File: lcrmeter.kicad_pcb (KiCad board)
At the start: 2 copper layers, 63.4 x 75.5 mm, 35 parts, among them J1 inductor, J2 inductor, J3 gen, J4 1,5V, J5 gen, J6 OSC, J7 OSC, SW1 power, SW2 +, SW3 -, SW4 ok, SW5 back, U1 MCP47, U2 STM32F103C8Tx, Y1 8Mhz

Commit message: assigned footprints, fixed schematic, a little done PCB
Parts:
- removed DIS1: nokia5110_LCD, Moje:LCD_5110
- removed L1: 10u, Inductors_SMD:L_0805_HandSoldering
- added C10: 100n, Capacitor_SMD:C_0603_1608Metric_Pad1.05x0.95mm_HandSolder, B.Cu at (137.4, 118.5)
- added C11: 2u2, Capacitor_SMD:C_0805_2012Metric_Pad1.15x1.40mm_HandSolder, B.Cu at (126.5, 177.5)
- added C12: 100n, Capacitor_SMD:C_0603_1608Metric_Pad1.05x0.95mm_HandSolder, B.Cu at (91.6, 141.0)
- added C13: 100n, Capacitor_SMD:C_0603_1608Metric_Pad1.05x0.95mm_HandSolder, B.Cu at (162.6, 142.6)
- added C14: 100n, Capacitor_SMD:C_0603_1608Metric_Pad1.05x0.95mm_HandSolder, B.Cu at (103.2, 155.9)
- added C15: 100n, Capacitor_SMD:C_0603_1608Metric_Pad1.05x0.95mm_HandSolder, B.Cu at (145.4, 166.1)
- added C8: 10u, Capacitor_SMD:C_0603_1608Metric_Pad1.05x0.95mm_HandSolder, B.Cu at (168.5, 138.2)
- added C9: 100n, Capacitor_SMD:C_0603_1608Metric_Pad1.05x0.95mm_HandSolder, B.Cu at (91.2, 148.7)
- added D1: BAT54S, Package_TO_SOT_SMD:SOT-23, B.Cu at (119.4, 105.9)
- added D2: BAT54S, Package_TO_SOT_SMD:SOT-23, B.Cu at (156.0, 109.7)
- added D3: BAT54S, Package_TO_SOT_SMD:SOT-23, B.Cu at (158.0, 114.0)
- added D4: BAT54S, Package_TO_SOT_SMD:SOT-23, B.Cu at (141.8, 106.4)
- added D5: BAT54S, Package_TO_SOT_SMD:SOT-23, B.Cu at (157.5, 106.2)
- added R10: 10k, Resistor_SMD:R_0603_1608Metric_Pad1.05x0.95mm_HandSolder, B.Cu at (133.0, 161.6)
- added R11: 10k, Resistor_SMD:R_0603_1608Metric_Pad1.05x0.95mm_HandSolder, B.Cu at (167.0, 141.0)
- added R12: 10k, Resistor_SMD:R_0603_1608Metric_Pad1.05x0.95mm_HandSolder, B.Cu at (87.9, 149.7)
- added R13: 10k, Resistor_SMD:R_0603_1608Metric_Pad1.05x0.95mm_HandSolder, B.Cu at (145.5, 141.1)
- added R14: 22, Resistor_SMD:R_0805_2012Metric_Pad1.15x1.40mm_HandSolder, B.Cu at (161.3, 119.6)
- added R15: 1k5, Resistor_SMD:R_0805_2012Metric_Pad1.15x1.40mm_HandSolder, B.Cu at (92.2, 163.6)
- added R16: 22, Resistor_SMD:R_0805_2012Metric_Pad1.15x1.40mm_HandSolder, B.Cu at (84.6, 153.1)
- added R17: 100, Resistor_SMD:R_0805_2012Metric_Pad1.15x1.40mm_HandSolder, B.Cu at (162.3, 114.3)
- added R18: 100, Resistor_SMD:R_0805_2012Metric_Pad1.15x1.40mm_HandSolder, B.Cu at (155.9, 163.3)
- added R9: 10k, Resistor_SMD:R_0603_1608Metric_Pad1.05x0.95mm_HandSolder, B.Cu at (151.3, 154.4)
- added U3: OLED, footprints:OLED_128x64, F.Cu at (153.4, 106.4)
- added U4: 74HC14, Package_SO:SOIC-14_3.9x8.7mm_P1.27mm, B.Cu at (126.3, 123.7)
- BT1, BT2: footprint Battery_Holders:Keystone_2466_1xAAA -> Battery:BatteryHolder_Keystone_2466_1xAAA
- C1, C2: footprint Capacitors_SMD:C_0805_HandSoldering -> Capacitor_SMD:C_0805_2012Metric_Pad1.15x1.40mm_HandSolder
- C3, C4, C5, C6: footprint Capacitors_SMD:C_0805_HandSoldering -> Capacitor_SMD:C_0603_1608Metric_Pad1.05x0.95mm_HandSolder; moved to B.Cu
- C7: value 10n -> 100n; footprint Capacitors_SMD:C_0805_HandSoldering -> Capacitor_SMD:C_0603_1608Metric_Pad1.05x0.95mm_HandSolder; moved to B.Cu
- J1: value inductor -> LCR_input; footprint Pin_Headers:Pin_Header_Straight_1x04_Pitch2.54mm -> Connector_PinHeader_2.54mm:PinHeader_1x04_P2.54mm_Vertical
- J2: value inductor -> LCR_input; footprint Socket_Strips:Socket_Strip_Straight_1x04_Pitch2.54mm -> Connector_PinSocket_2.54mm:PinSocket_1x04_P2.54mm_Vertical
- J3: value gen -> Conn_01x06; footprint Socket_Strips:Socket_Strip_Straight_1x02_Pitch2.54mm -> Connector_PinHeader_2.54mm:PinHeader_1x06_P2.54mm_Vertical
- J4: value 1,5V -> USB_B_Micro; footprint Socket_Strips:Socket_Strip_Straight_1x02_Pitch2.54mm -> Connector_USB:USB_Micro-B_Molex_47346-0001
- J5: value gen -> OSCILLOSCOPE; footprint Pin_Headers:Pin_Header_Straight_1x02_Pitch2.54mm -> footprints:BNC TE CONNECTIVITY 5-1634503
- J6: value OSC -> misc; footprint Socket_Strips:Socket_Strip_Straight_1x02_Pitch2.54mm -> Connector_PinSocket_2.54mm:PinSocket_1x06_P2.54mm_Vertical
- J7: value OSC -> misc; footprint Pin_Headers:Pin_Header_Straight_1x02_Pitch2.54mm -> Connector_PinHeader_2.54mm:PinHeader_1x06_P2.54mm_Vertical
- L2: footprint Inductors_SMD:L_0805_HandSoldering -> Inductor_SMD:L_0805_2012Metric_Pad1.15x1.40mm_HandSolder; moved to B.Cu
- R1: value R -> 100; footprint Resistors_SMD:R_0805_HandSoldering -> Resistor_SMD:R_0805_2012Metric_Pad1.15x1.40mm_HandSolder; moved to B.Cu
- R2: value 4K7 -> 10k; footprint Resistors_SMD:R_0805_HandSoldering -> Resistor_SMD:R_0603_1608Metric_Pad1.05x0.95mm_HandSolder; moved to B.Cu
- R3, R4, R5, R6: footprint Resistors_SMD:R_0805_HandSoldering -> Resistor_SMD:R_0603_1608Metric_Pad1.05x0.95mm_HandSolder
- R7, R8: footprint Resistors_SMD:R_0805_HandSoldering -> Resistor_SMD:R_0805_2012Metric_Pad1.15x1.40mm_HandSolder; moved to B.Cu
- SW1: footprint Pin_Headers:Pin_Header_Straight_1x03_Pitch2.54mm -> Connector_PinHeader_2.54mm:PinHeader_1x03_P2.54mm_Vertical
- SW2, SW3, SW4, SW5: footprint Buttons_Switches_SMD:SW_SPST_REED_CT05-XXXX-G1 -> Button_Switch_SMD:SW_SPST_REED_CT05-XXXX-G1
- U1: footprint Housings_SSOP:TSSOP-8_4.4x3mm_Pitch0.65mm -> Package_SO:TSSOP-8_4.4x3mm_P0.65mm; moved to B.Cu
- U2: footprint Housings_QFP:LQFP-48_7x7mm_Pitch0.5mm -> Package_QFP:LQFP-48_7x7mm_P0.5mm; moved to B.Cu
- Y1: footprint Crystals:Crystal_HC49-U_Vertical -> Crystal:Crystal_HC49-U_Vertical; moved to F.Cu
- moved C6 73.5 mm to (99.8, 154.4), turned to 0 degrees
- moved R4 70.5 mm to (129.3, 156.0), turned to 0 degrees
- moved C5 69.5 mm to (106.3, 162.0)
- moved L2 66.6 mm to (112.8, 177.5), turned to 0 degrees
- moved C7 65.0 mm to (106.3, 163.5), turned to 0 degrees
- moved SW2 61.3 mm to (140.7, 137.2), turned to 0 degrees
- moved R3 60.3 mm to (138.1, 153.9), turned to 0 degrees
- moved SW3 60.2 mm to (140.7, 144.8), turned to 0 degrees
- moved BT1 59.7 mm to (126.1, 144.3), turned to 90 degrees
- moved C4 58.8 mm to (109.7, 165.5), turned to 0 degrees
- moved J5 56.5 mm to (169.9, 102.4), turned to 0 degrees
- moved R2 40.5 mm to (149.6, 109.6), turned to 270 degrees
- moved U1 39.4 mm to (138.4, 111.5)
- moved SW4 38.0 mm to (154.9, 141.2), turned to 0 degrees
- moved R6 37.3 mm to (149.5, 135.1)
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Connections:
- J1 pad 1: Net-(J1-Pad1) -> /ADC_2
- J1 pad 2: Net-(J1-Pad1) -> /ADC_2
- J2 pad 1: Net-(J1-Pad1) -> /ADC_2
- J2 pad 2: Net-(J1-Pad1) -> /ADC_2
- J3 pad 1: GND -> VCC
- J4 pad 1: +1V5 -> /VBUS
- J4 pad 2: +1V5 -> Net-(J4-Pad2)
- J5 pad 1: Net-(J3-Pad2) -> Net-(J5-Pad1)
- J6 pad 1: OSC -> /PWM_OUT
- J6 pad 2: GND -> /8_MHz_OUT
- J7 pad 1: OSC -> /PWM_OUT
- J7 pad 2: GND -> /8_MHz_OUT
- R1 pad 1: Net-(J3-Pad2) -> /ADC_1
- R1 pad 2: Net-(J1-Pad1) -> /ADC_2
- R2 pad 1: VCC -> GND
- R3 pad 1: Net-(R3-Pad1) -> GND
- R3 pad 2: GND -> Net-(R3-Pad2)
- R4 pad 1: Net-(R4-Pad1) -> VCC
- R4 pad 2: GND -> Net-(R10-Pad2)
- R5 pad 1: Net-(R5-Pad1) -> VCC
- R5 pad 2: GND -> Net-(R11-Pad2)
- R6 pad 1: Net-(R6-Pad1) -> VCC
- R6 pad 2: GND -> Net-(R12-Pad2)
- R7 pad 2: Net-(R7-Pad2) -> /I2C_SCL
- R8 pad 2: Net-(R8-Pad2) -> /I2C_SDA
- SW1 pad 3: Net-(L1-Pad2) -> VCC
- SW2 pad 1: Net-(R3-Pad1) -> GND
- SW2 pad 2: VCC -> Net-(R12-Pad2)
- SW3 pad 1: Net-(R4-Pad1) -> GND
- SW3 pad 2: VCC -> Net-(R13-Pad2)
- SW4 pad 1: Net-(R5-Pad1) -> GND
- SW4 pad 2: VCC -> Net-(R10-Pad2)
- SW5 pad 1: Net-(R6-Pad1) -> GND
- SW5 pad 2: VCC -> Net-(R11-Pad2)
- U1 pad 3: Net-(J3-Pad2) -> /ADC_1
- U1 pad 6: GND -> /LATCH
- U1 pad 7: Net-(R8-Pad2) -> /I2C_SCL
- U1 pad 8: Net-(R7-Pad2) -> /I2C_SDA
- U2 pad 1: (no net) -> VCC
- U2 pad 12: Net-(DIS1-Pad1) -> /BUTTON_OK
- U2 pad 13: Net-(DIS1-Pad3) -> /BUTTON_BACK
- U2 pad 14: Net-(DIS1-Pad2) -> /BUTTON_-
- U2 pad 15: Net-(DIS1-Pad5) -> /BUTTON_+
- U2 pad 16: Net-(DIS1-Pad4) -> (no net)
- U2 pad 17: OSC -> /OSCILLOSCOPE
- U2 pad 18: Net-(J1-Pad1) -> /ADC_1
- U2 pad 19: Net-(J3-Pad2) -> /ADC_2
- U2 pad 20: GND -> Net-(R2-Pad2)
- U2 pad 21: (no net) -> Net-(U2-Pad21)
- U2 pad 22: (no net) -> Net-(U2-Pad22)
- U2 pad 29: (no net) -> /8_MHz_OUT
- U2 pad 30: (no net) -> /PWM_OUT
- U2 pad 31: (no net) -> /VBUS
- U2 pad 32: (no net) -> /USB_-
- U2 pad 33: Net-(R3-Pad1) -> /USB_+
- U2 pad 34: Net-(R4-Pad1) -> Net-(J3-Pad2)
- U2 pad 37: Net-(R5-Pad1) -> Net-(J3-Pad3)
- U2 pad 38: Net-(R6-Pad1) -> /USB_EN
- U2 pad 39: (no net) -> /SWO
- U2 pad 41: (no net) -> /LATCH
- U2 pad 42: Net-(R8-Pad2) -> /I2C_SCL
- U2 pad 43: Net-(R7-Pad2) -> /I2C_SDA
- U2 pad 44: GND -> Net-(R3-Pad2)
- U2 pad 7: Net-(R2-Pad2) -> /RST
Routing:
- net GND: track 376.2 -> 0.00 mm, vias 2 -> 0
- net VCC: track 142.6 -> 0.00 mm
- net +1V5: track 77.9 -> 0.00 mm
- net Net-(J3-Pad2): track 56.3 -> 0.00 mm, vias 3 -> 0
- net Net-(R3-Pad1): track 51.8 -> 0.00 mm, vias 3 -> 0
- net Net-(J1-Pad1): track 50.9 -> 0.00 mm, vias 2 -> 0
- net Net-(R4-Pad1): track 50.4 -> 0.00 mm, vias 2 -> 0
- net Net-(R5-Pad1): track 42.4 -> 0.00 mm, vias 2 -> 0
- net Net-(R6-Pad1): track 41.3 -> 0.00 mm, vias 2 -> 0
- net OSC: track 37.3 -> 0.00 mm, vias 1 -> 0
- net VDDA: track 32.6 -> 0.00 mm, vias 4 -> 0
- net Net-(DIS1-Pad1): track 31.4 -> 0.00 mm
- net Net-(DIS1-Pad4): track 27.5 -> 0.00 mm
- net Net-(R7-Pad2): track 25.6 -> 0.00 mm
- net Net-(DIS1-Pad5): track 22.8 -> 0.00 mm
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- removed copper zone on B.Cu, net GND
- removed copper zone on F.Cu, net GND
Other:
- board outline removed
- net class Default: via_dia 0.6 -> 0.8
- rule pad_to_mask_clearance: 0.1 -> 0
- board text removed: "+"
- board text removed: "-"
- board text removed: "1,5 V"
- board text removed: "BACK"
- board text removed: "GENERATOR"
- board text removed: "INDUCTOR"
- board text removed: "OK"
- board text removed: "OSCILISCOPE"

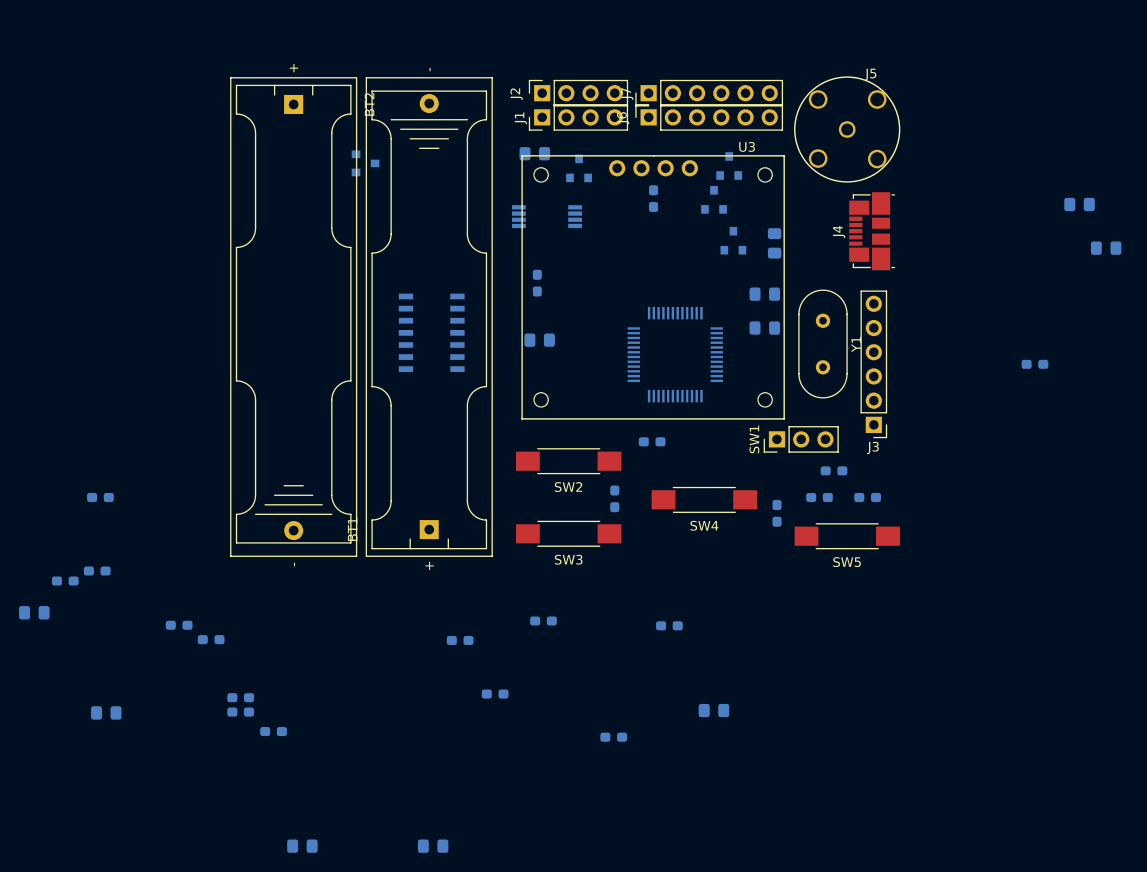
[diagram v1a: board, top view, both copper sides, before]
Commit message: started routing added voltage divider for measuring supply foltage
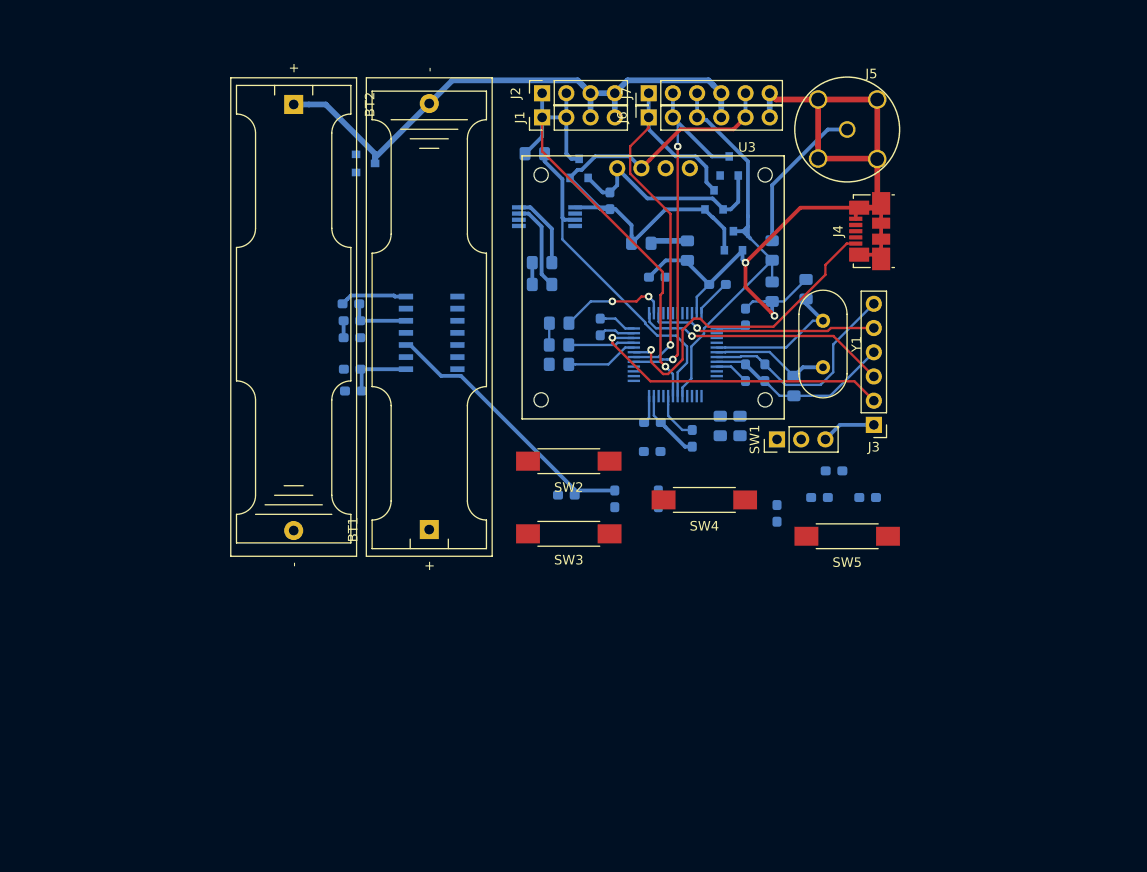
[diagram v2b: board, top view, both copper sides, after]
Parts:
- added R19: 20k, Resistor_SMD:R_0805_2012Metric_Pad1.15x1.40mm_HandSolder, B.Cu at (158.7, 133.5)
- added R20: 10k, Resistor_SMD:R_0805_2012Metric_Pad1.15x1.40mm_HandSolder, B.Cu at (156.6, 133.5)
- moved C9 73.0 mm to (159.3, 122.0), turned to 90 degrees
- moved L2 72.6 mm to (148.3, 114.3)
- moved C11 67.9 mm to (153.2, 115.1), turned to 270 degrees
- moved C5 66.2 mm to (156.3, 118.6), turned to 180 degrees
- moved C7 63.8 mm to (159.3, 127.9), turned to 90 degrees
- moved C6 63.4 mm to (145.0, 109.8), turned to 90 degrees
- moved R15 62.7 mm to (139.7, 122.7), turned to 180 degrees
- moved R16 61.8 mm to (139.7, 125.0)
- moved C4 54.6 mm to (144.0, 123.1), turned to 270 degrees
- moved R18 44.4 mm to (162.1, 119.4), turned to 270 degrees
- moved R10 41.9 mm to (118.0, 122.4), turned to 180 degrees
- moved C3 40.6 mm to (149.5, 133.1), turned to 0 degrees
- moved R3 38.0 mm to (150.0, 117.9)
- moved R12 37.4 mm to (118.0, 127.5), turned to 180 degrees
- moved C1 35.5 mm to (164.3, 129.3), turned to 270 degrees
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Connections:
- J4 pad 4: (no net) -> Net-(J4-Pad4)
- SW1 pad 1: (no net) -> Net-(SW1-Pad1)
- U1 pad 4: (no net) -> Net-(U1-Pad4)
- U2 pad 10: (no net) -> Net-(U2-Pad10)
- U2 pad 11: (no net) -> Net-(R19-Pad2)
- U2 pad 16: (no net) -> Net-(U2-Pad16)
- U2 pad 2: (no net) -> Net-(U2-Pad2)
- U2 pad 25: (no net) -> Net-(U2-Pad25)
- U2 pad 26: (no net) -> Net-(U2-Pad26)
- U2 pad 27: (no net) -> Net-(U2-Pad27)
- U2 pad 28: (no net) -> Net-(U2-Pad28)
- U2 pad 3: (no net) -> Net-(U2-Pad3)
- U2 pad 4: (no net) -> Net-(U2-Pad4)
- U2 pad 40: (no net) -> Net-(U2-Pad40)
- U2 pad 45: (no net) -> Net-(U2-Pad45)
- U2 pad 46: (no net) -> Net-(U2-Pad46)
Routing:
- net GND: track 0.00 -> 160.7 mm, vias 0 -> 2
- net VCC: track 0.00 -> 75.3 mm
- net +1V5: track 0.00 -> 61.3 mm
- net /ADC_2: track 0.00 -> 52.7 mm, vias 0 -> 1
- net /PWM_OUT: track 0.00 -> 45.0 mm, vias 0 -> 1
- net /OSCILLOSCOPE: track 0.00 -> 44.4 mm
- net /8_MHz_OUT: track 0.00 -> 40.2 mm, vias 0 -> 2
- net /ADC_1: track 0.00 -> 34.6 mm
- net /VBUS: track 0.00 -> 34.0 mm, vias 0 -> 1
- net Net-(J3-Pad2): track 0.00 -> 32.8 mm, vias 0 -> 1
- net Net-(C15-Pad1): track 0.00 -> 29.0 mm
- net Net-(J3-Pad3): track 0.00 -> 26.8 mm, vias 0 -> 1
- net /SWO: track 0.00 -> 24.1 mm, vias 0 -> 1
- net /RST: track 0.00 -> 23.0 mm
- net Net-(J5-Pad1): track 0.00 -> 16.1 mm
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
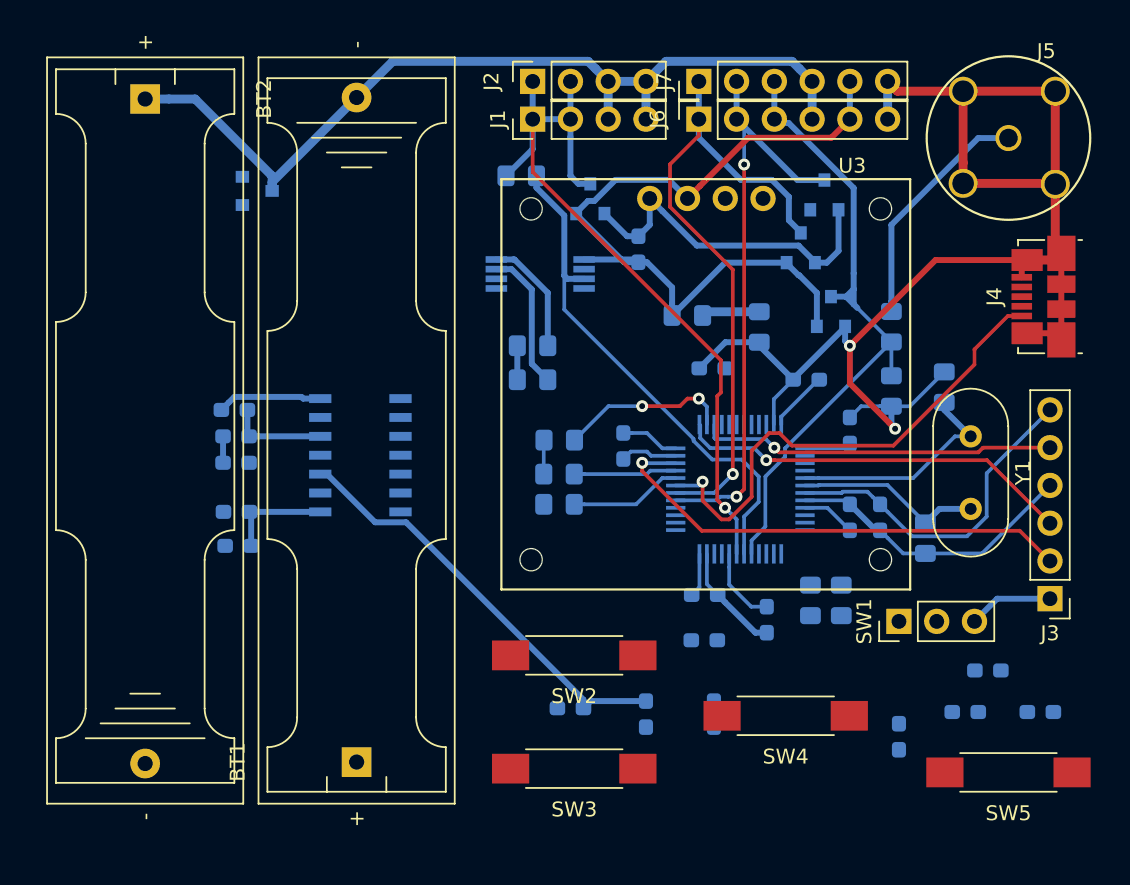
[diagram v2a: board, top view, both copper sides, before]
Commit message: fixed resistors value, PCB done!
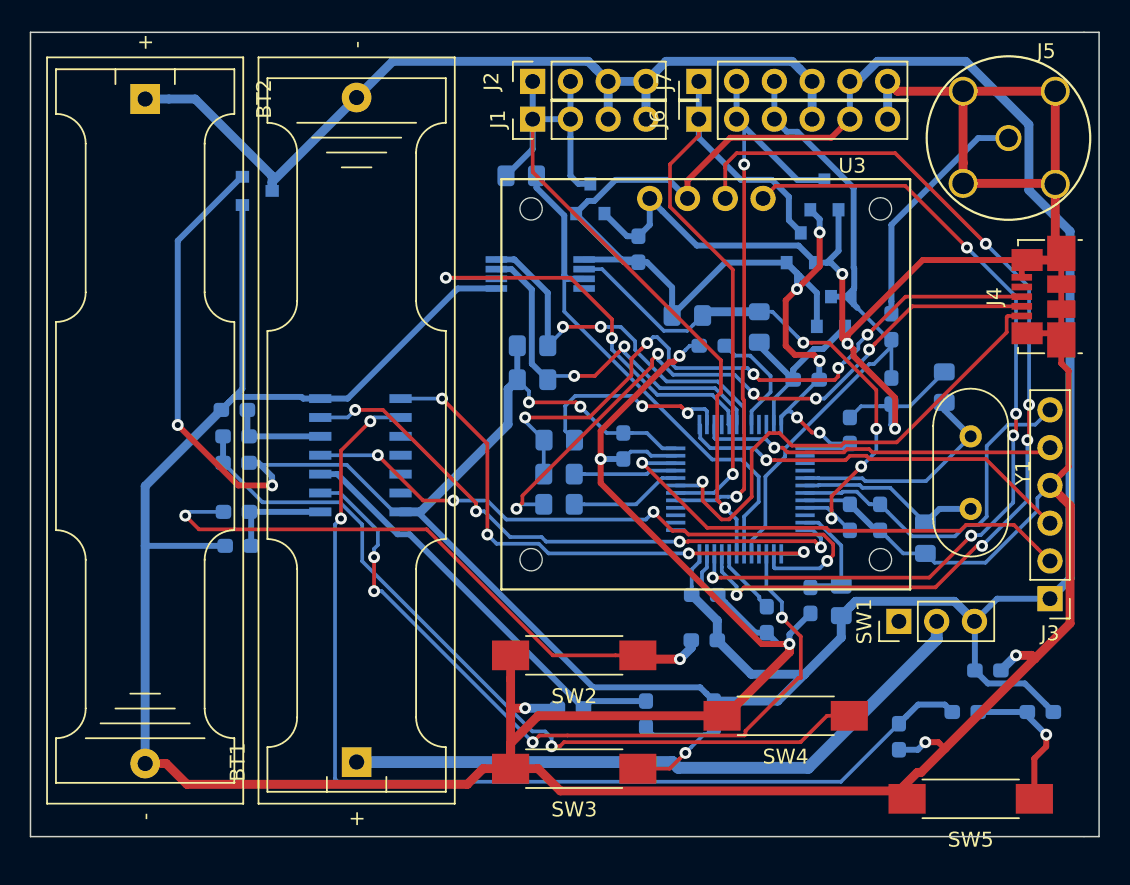
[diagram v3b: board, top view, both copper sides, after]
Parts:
- R17, R18: value 100 -> 10k; footprint Resistor_SMD:R_0805_2012Metric_Pad1.15x1.40mm_HandSolder -> Resistor_SMD:R_0603_1608Metric_Pad1.05x0.95mm_HandSolder
- R20: footprint Resistor_SMD:R_0805_2012Metric_Pad1.15x1.40mm_HandSolder -> Resistor_SMD:R_0603_1608Metric_Pad1.05x0.95mm_HandSolder
- moved SW5 3.10 mm to (167.4, 146.8)
- moved R3 1.52 mm to (150.0, 116.3)
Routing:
- net GND: track 160.7 -> 390.1 mm, vias 2 -> 9
- net VCC: track 75.3 -> 276.2 mm, vias 0 -> 9
- net Net-(C13-Pad1): track 0.00 -> 71.1 mm, vias 0 -> 2
- net Net-(U2-Pad21): track 0.00 -> 66.5 mm, vias 0 -> 5
- net Net-(U2-Pad22): track 0.00 -> 58.3 mm, vias 0 -> 5
- net /BUTTON_+: track 0.00 -> 53.2 mm, vias 0 -> 4
- net Net-(R10-Pad2): track 1.78 -> 54.4 mm, vias 0 -> 1
- net Net-(J4-Pad2): track 0.00 -> 45.0 mm, vias 0 -> 5
- net Net-(BT1-Pad1): track 0.00 -> 44.0 mm
- net /BUTTON_-: track 0.00 -> 43.4 mm, vias 0 -> 4
- net Net-(J4-Pad3): track 2.29 -> 45.2 mm, vias 0 -> 5
- net Net-(R12-Pad2): track 0.00 -> 41.5 mm, vias 0 -> 2
- net /BUTTON_OK: track 0.00 -> 40.0 mm, vias 0 -> 4
- net /BUTTON_BACK: track 0.00 -> 36.6 mm, vias 0 -> 4
- net VDDA: track 7.56 -> 37.9 mm, vias 0 -> 4
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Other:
- board outline added: 71.9 x 54.1 mm

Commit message: deleted 1,5V diode protection, added op-amp for 1,5V(optional), added zones
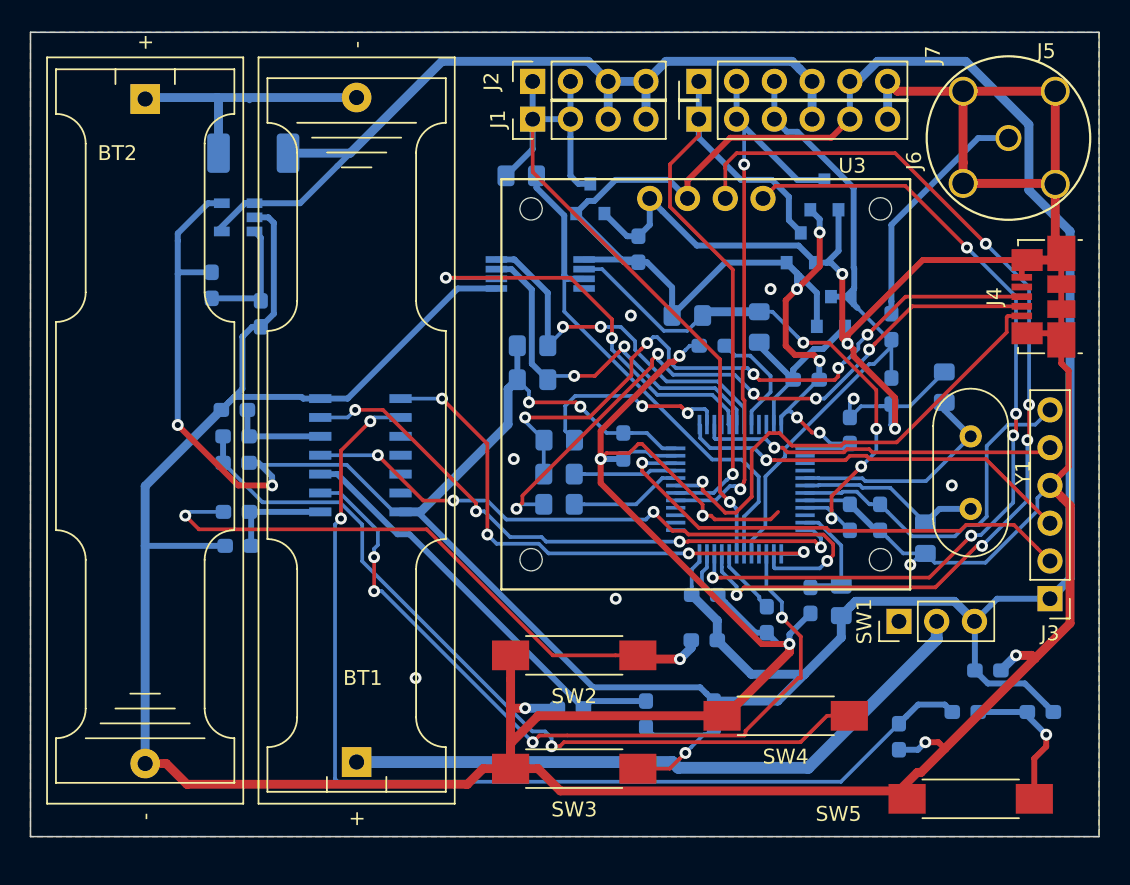
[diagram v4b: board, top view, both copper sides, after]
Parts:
- removed D1: BAT54S, Package_TO_SOT_SMD:SOT-23
- added R21: 0, Resistor_SMD:R_2010_5025Metric_Pad1.52x2.65mm_HandSolder, B.Cu at (119.1, 103.4)
- added R22: 10k, Resistor_SMD:R_0603_1608Metric_Pad1.05x0.95mm_HandSolder, B.Cu at (116.3, 112.3)
- added R23: 10k, Resistor_SMD:R_0603_1608Metric_Pad1.05x0.95mm_HandSolder, B.Cu at (119.6, 114.2)
- added U5: MCP6001-OT, Package_TO_SOT_SMD:SOT-23-5, B.Cu at (118.1, 107.7)
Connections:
- BT1 pad 2: +1V5 -> Net-(BT1-Pad2)
- BT2 pad 1: +1V5 -> Net-(BT1-Pad2)
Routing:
- net Net-(BT1-Pad2): track 0.00 -> 32.5 mm
- net GND: track 390.1 -> 409.3 mm, vias 9 -> 18
- net Net-(R22-Pad2): track 0.00 -> 8.21 mm
- net +1V5: track 61.3 -> 67.0 mm
- net /VBUS: track 34.0 -> 33.2 mm
- added copper zone on B.Cu, net GND
- added copper zone on F.Cu, net GND
